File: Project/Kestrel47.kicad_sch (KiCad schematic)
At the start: 96 parts, among them SW1 SW_Push, U1 ProMicro

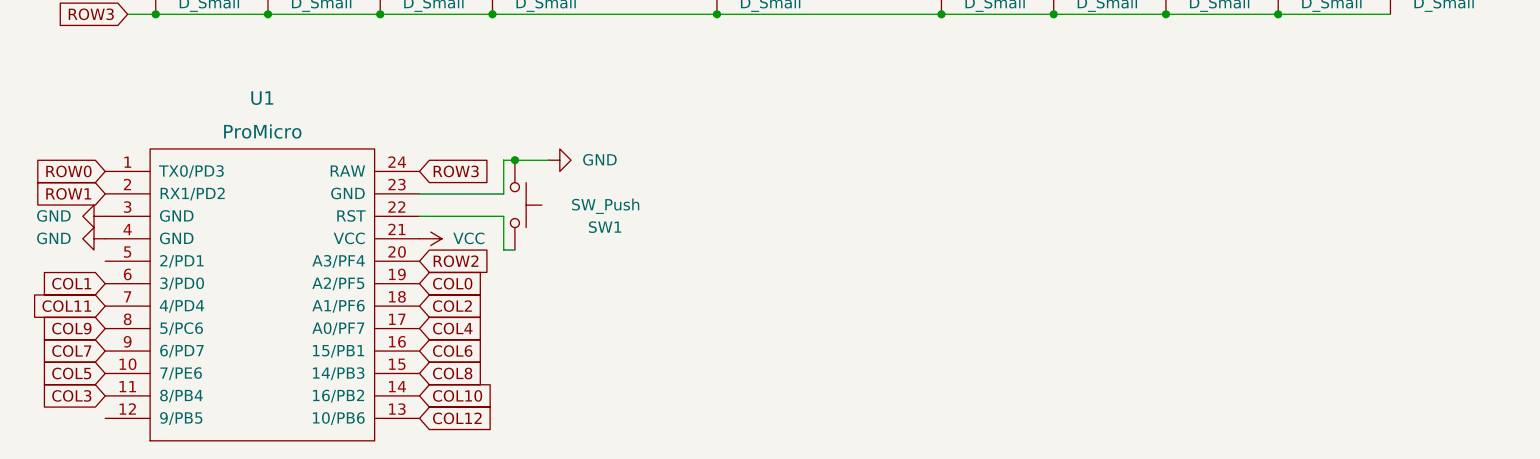
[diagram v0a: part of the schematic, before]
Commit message: rerouting mistake, adding rgb and power button
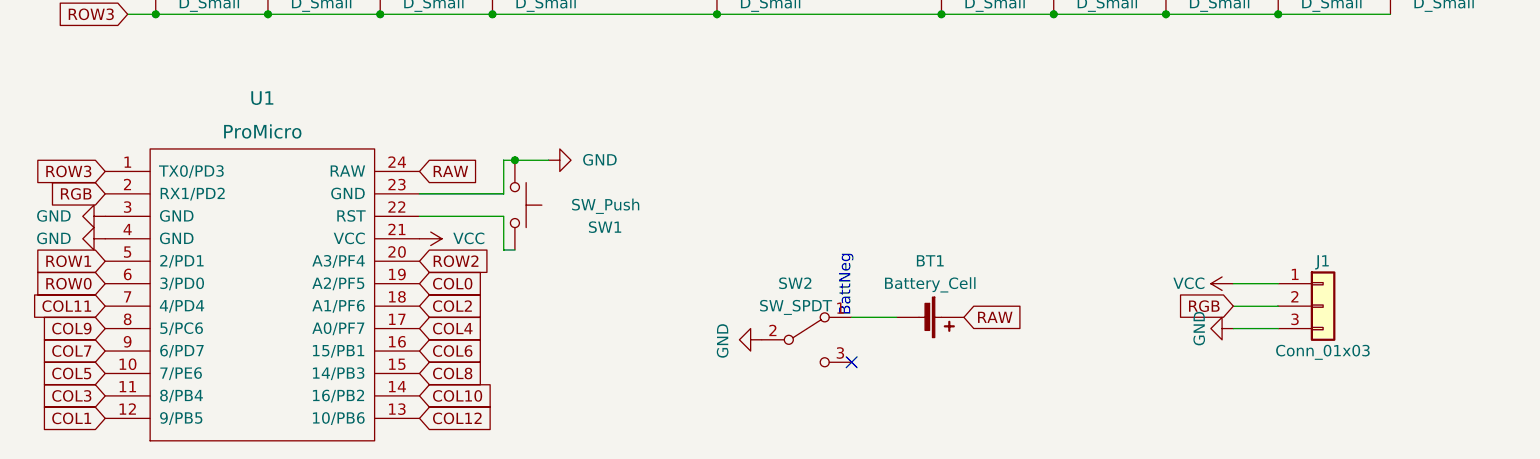
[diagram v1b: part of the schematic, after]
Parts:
- added BT1: Battery_Cell, keeblib:cell_pads, symbol Device:Battery_Cell
- added J1: Conn_01x03, Connector_PinSocket_2.00mm:PinSocket_1x03_P2.00mm_Vertical, symbol alpha_pro_micro-rescue:Conn_01x03
- added SW2: SW_SPDT, keeblib:switch_SSSS811101, symbol Switch:SW_SPDT
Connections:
- net  ROW3: now also U1.1 (TX0/PD3); no longer U1.24 (RAW)
- net COL1: now also U1.12 (9/PB5); no longer U1.6 (3/PD0)
- net GND: now also J1.3 (Pin_3), SW2.2 (B)
- net ROW0: now also U1.6 (3/PD0); no longer U1.1 (TX0/PD3)
- net ROW1: now also U1.5 (2/PD1); no longer U1.2 (RX1/PD2)
- net VCC: now also J1.1 (Pin_1)
- new net: BT1.2 (-), SW2.1 (A)
- new net RAW: BT1.1 (+), U1.24 (RAW)
- new net RGB: J1.2 (Pin_2), U1.2 (RX1/PD2)
- no-connect marks 0 -> 1
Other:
- note added: "BattNeg"
